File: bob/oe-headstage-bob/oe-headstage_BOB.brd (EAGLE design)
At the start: 160 x 100 mm, 24 parts, among them U1 SN65LVDS1DBVR, U2 SN65LVDS2DBVR, U3 SN65LVDS1DBVR, U4 SN65LVDS2DBVR, U5 SN65LVDS1DBVR, U6 SN65LVDS1DBVR

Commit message: Working through LVDS BOB, still.
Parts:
- removed S1, S2: RHD2000-CABLE-DAQ-SIDE, RHD2000_eval_board:OMNETICS_PZN-12-AA
- added U$1, U$2: RHD2000-CABLE-DAQ-SIDE-SINGLE, puggleboard:OMNETICS_PZN_12_AA-SINGLEBUS
- moved C10 2.40 mm to (24.4, 26.7)
- moved C11 2.40 mm to (15.5, 19.1)
- moved C12 2.40 mm to (24.4, 19.1)
- moved C3 2.40 mm to (17.0, 26.7)
- moved C4 2.40 mm to (25.9, 26.7)
- moved C5 2.40 mm to (17.0, 19.1)
- moved C6 2.40 mm to (25.9, 19.1)
- moved C9 2.40 mm to (15.5, 26.7)
- moved C1 2.40 mm to (15.5, 34.3)
- moved C7 2.40 mm to (17.0, 34.3)
- moved R2 1.83 mm to (31.0, 27.9)
- moved U1 1.63 mm to (19.3, 35.6)
- moved U3 1.63 mm to (19.3, 27.9)
- moved U5 1.63 mm to (19.3, 20.3)
- moved U4 1.63 mm to (28.2, 27.9)
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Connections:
- net DIO_7 renamed DIO7
- removed net DIO_6: D_I/O.14
- new net DIO1: D_I/O.2
- net CS1: now also D_I/O.8; no longer D_I/O.6
- net CS1_N: now also U$1.T1; no longer S1.T1
- net CS1_P: now also U$1.B1; no longer S1.B1
- net CS2: now also D_I/O.14; no longer D_I/O.10
- net CS2_N: now also U$2.T1; no longer S2.T1
- net CS2_P: now also U$2.B1; no longer S2.B1
- net GND: now also U$1.T6, U$2.T6; no longer S1.T6, S2.T6
- net MISO1_N: now also U$1.T4; no longer S1.T4
- net MISO1_P: now also U$1.B4; no longer S1.B4
- net MISO2: now also D_I/O.10; no longer D_I/O.8
- net MISO2_N: now also U$2.T4; no longer S2.T4
- net MISO2_P: now also U$2.B4; no longer S2.B4
- net MOSI_N: now also U$1.T3, U$2.T3; no longer S1.T3, S2.T3
- net MOSI_P: now also U$1.B3, U$2.B3; no longer S1.B3, S2.B3
- net SCLK: now also D_I/O.6; no longer D_I/O.2
- net SCLK_N: now also U$1.T2, U$2.T2; no longer S1.T2, S2.T2
- net SCLK_P: now also U$1.B2, U$2.B2; no longer S1.B2, S2.B2
- net VDRIVE: now also U$1.B6, U$2.B6; no longer S1.B6, S2.B6
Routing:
- net VDRIVE: track 64.5 -> 2.77 mm, vias 6 -> 1
- net VDRIVE1: track 57.2 -> 0.00 mm, vias 6 -> 0
- net SCLK_P1: track 0.00 -> 25.7 mm, vias 0 -> 3
- net SCLK_N1: track 0.00 -> 19.0 mm, vias 0 -> 1
- net MOSI_N: track 0.00 -> 19.0 mm, vias 0 -> 2
- net CS2_P: track 0.00 -> 15.2 mm
- net SCLK_P: track 17.3 -> 31.5 mm, vias 0 -> 2
- net CS2_N: track 0.00 -> 13.2 mm
- net SCLK_N: track 15.1 -> 28.1 mm
- net MISO1_P: track 0.00 -> 12.4 mm
- net MOSI_P: track 0.00 -> 11.8 mm
- net MISO1_N: track 0.00 -> 10.6 mm
- net MISO1_P3: track 0.00 -> 9.97 mm, vias 0 -> 2
- net MISO1_P2: track 0.00 -> 9.97 mm, vias 0 -> 2
- net MISO1_P1: track 0.00 -> 9.97 mm, vias 0 -> 2
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
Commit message: Working through LVDS BOB, still.
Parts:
- added R3, R4, R5, R6, R7, R8: 0, puggleboard:0603
- moved R1 16.6 mm to (25.1, 20.1)
- moved U1 16.6 mm to (13.5, 20.1)
- moved U2 16.6 mm to (22.4, 20.1)
- moved C1 16.6 mm to (9.65, 18.8)
- moved C10 16.6 mm to (18.5, 11.2)
- moved C11 16.6 mm to (9.65, 3.56)
- moved C12 16.6 mm to (18.5, 3.56)
- moved C13 16.6 mm to (2.79, 22.6)
- moved C2 16.6 mm to (18.5, 18.8)
- moved C3 16.6 mm to (11.2, 11.2)
- moved C4 16.6 mm to (20.1, 11.2)
- moved C5 16.6 mm to (11.2, 3.56)
- moved C6 16.6 mm to (20.1, 3.56)
- moved C7 16.6 mm to (11.2, 18.8)
- moved C8 16.6 mm to (20.1, 18.8)
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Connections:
- new net N$2: R4.1, U2.5
- new net N$3: R5.1, U3.5
- new net N$4: R6.1, U4.5
- new net N$5: R7.1, U5.5
- new net N$6: R8.1, U6.5
- new net N$7: R3.1, U1.5
- net CS1: now also R5.2; no longer U3.5
- net CS2: now also R7.2; no longer U5.5
- net MISO1: now also R4.2; no longer U2.5
- net MISO2: now also R6.2; no longer U4.5
- net MOSI: now also R8.2; no longer U6.5
- net SCLK: now also R3.2; no longer U1.5
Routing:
- net VDRIVE: track 2.77 -> 61.5 mm, vias 1 -> 2
- net SCLK_P1: track 25.7 -> 0.00 mm, vias 3 -> 0
- net MOSI_P: track 11.8 -> 34.0 mm, vias 0 -> 3
- net SCLK_N1: track 19.0 -> 0.00 mm, vias 1 -> 0
- net MISO1: track 0.00 -> 17.8 mm
- net MISO2_P: track 2.40 -> 20.1 mm
- net MISO2: track 0.00 -> 16.8 mm
- net MISO2_N: track 3.07 -> 19.8 mm
- net MOSI_N: track 19.0 -> 35.4 mm, vias 2 -> 4
- net CS2_N: track 13.2 -> 29.6 mm
- net SCLK_N: track 28.1 -> 43.9 mm, vias 0 -> 4
- net CS2_P: track 15.2 -> 30.2 mm, vias 0 -> 2
- net MOSI: track 0.00 -> 14.6 mm
- net SCLK_P: track 31.5 -> 44.2 mm
- net MISO1_P3: track 9.97 -> 0.00 mm, vias 2 -> 0
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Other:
- board size 160 x 100 mm -> 43.4 x 25.7 mm

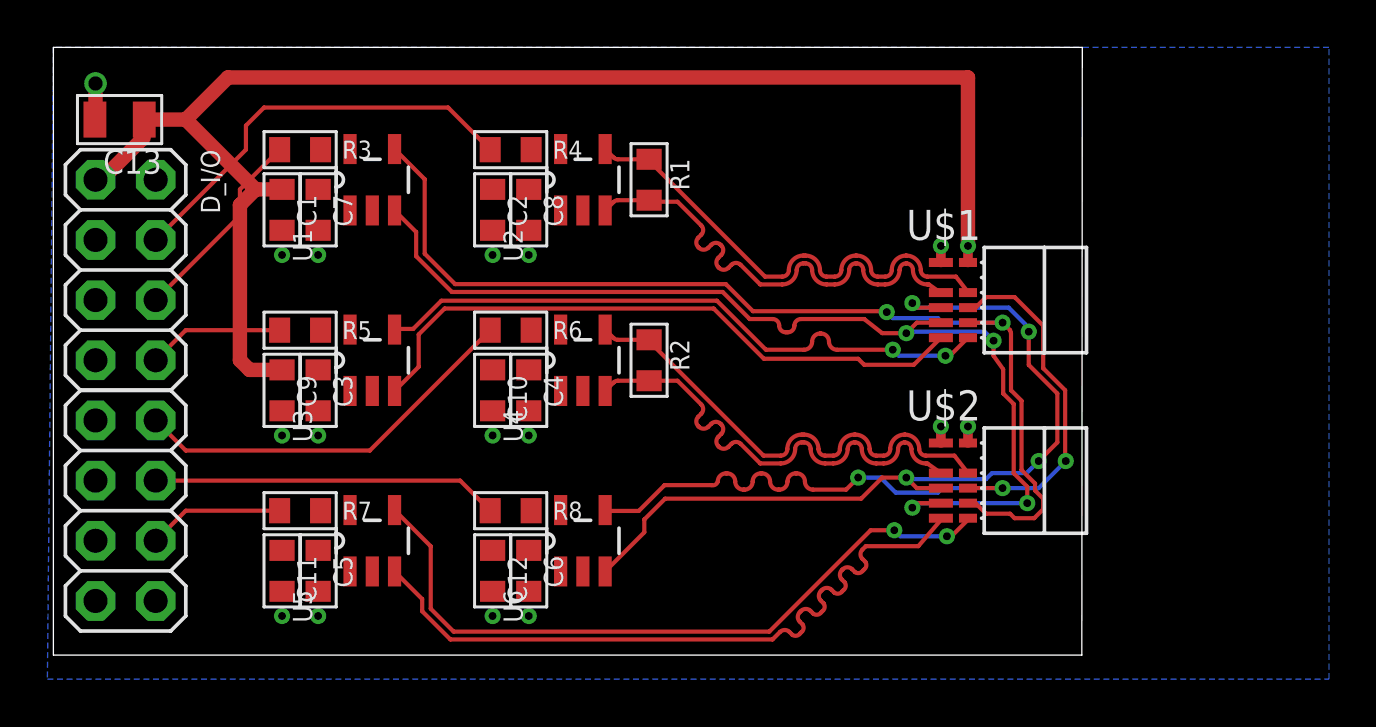
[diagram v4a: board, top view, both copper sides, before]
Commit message: All that needs to be done is silk-screen work.
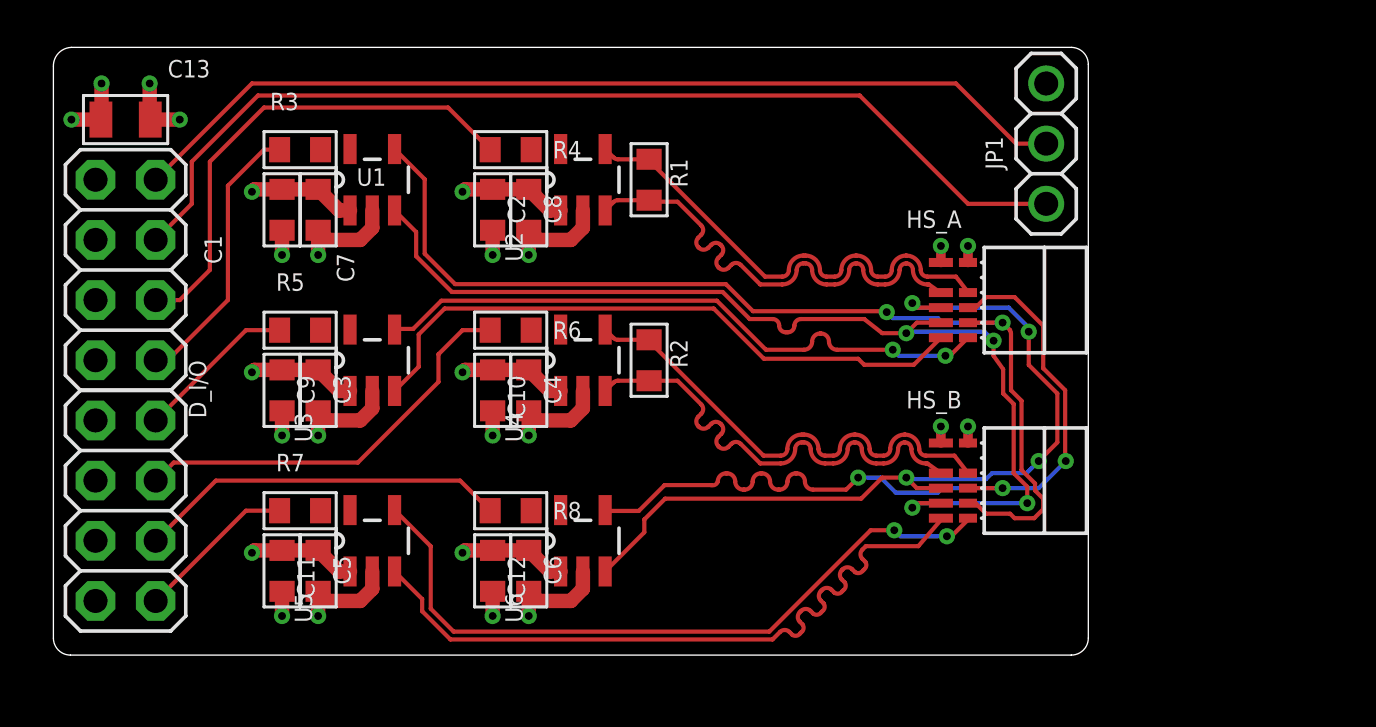
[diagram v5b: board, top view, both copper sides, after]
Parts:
- added JP1: (no value), adafruit:1X03
- U1, U3, U5, U6: value SN65LVDS1DBVR -> SN65LVDS1
- U2, U4: value SN65LVDS2DBVR -> SN65LVDS2
- moved C13 0.25 mm to (3.05, 22.6), turned to 0 degrees
- renumbered U$1 to HS_A, U$2 to HS_B
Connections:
- removed net DIO7: D_I/O.16
- new net DIO0: D_I/O.2, JP1.2
- net CS1: now also D_I/O.10; no longer D_I/O.8
- net CS2: now also D_I/O.16; no longer D_I/O.14
- net DIO1: now also D_I/O.4, JP1.1; no longer D_I/O.2
- net GND: now also JP1.3
- net MISO1: now also D_I/O.6; no longer D_I/O.4
- net MISO2: now also D_I/O.12; no longer D_I/O.10
- net MOSI: now also D_I/O.14; no longer D_I/O.12
- net SCLK: now also D_I/O.8; no longer D_I/O.6
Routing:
- net DIO1: track 0.00 -> 43.1 mm
- net DIO0: track 0.00 -> 40.3 mm
- net GND: track 2.95 -> 37.1 mm, vias 15 -> 16
- net VDRIVE: track 61.5 -> 31.5 mm, vias 2 -> 10
- net SCLK: track 8.52 -> 11.7 mm
- net MISO1: track 17.8 -> 20.9 mm
- net MOSI: track 14.6 -> 15.7 mm
- net CS2: track 5.76 -> 6.81 mm
- net CS1: track 5.76 -> 6.81 mm
- net MISO2: track 16.8 -> 17.4 mm
- added copper zone on layer 2, net GND
- added copper zone on layer 15, net VDRIVE
- removed copper zone on layer 16, net GND
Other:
- board size 43.4 x 25.7 mm -> 43.7 x 25.7 mm

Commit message: LDVS conversion board complete.
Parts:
- moved C11 1.52 mm to (11.2, 3.56)
- moved C3 1.52 mm to (9.65, 11.2)
- moved C5 1.52 mm to (9.65, 3.56)
- moved C9 1.52 mm to (11.2, 11.2)
- moved C10 1.52 mm to (20.1, 11.2)
- moved C12 1.52 mm to (20.1, 3.56)
- moved C4 1.52 mm to (18.5, 11.2)
- moved C6 1.52 mm to (18.5, 3.56)
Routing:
- net GND: track 37.1 -> 38.6 mm
- net N$7: track 0.00 -> 1.26 mm
- net N$3: track 0.00 -> 1.26 mm
- net N$5: track 0.00 -> 1.26 mm
- net N$4: track 0.00 -> 1.26 mm
- net N$2: track 0.00 -> 1.26 mm
- net N$6: track 0.00 -> 1.26 mm
